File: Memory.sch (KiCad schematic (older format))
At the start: 22 parts, among them U10 74LS05, U11 74HCT00, U12 74LS27, U13 74HC74, U14 74HC86, U2 AS6C4008-55PCN, U3 AS6C4008-55PCN, U4 AS6C4008-55PCN, U5 AS6C4008-55PCN, U6 74HCT00, U7 74LS32, U8 74LS32, U9 74LS05

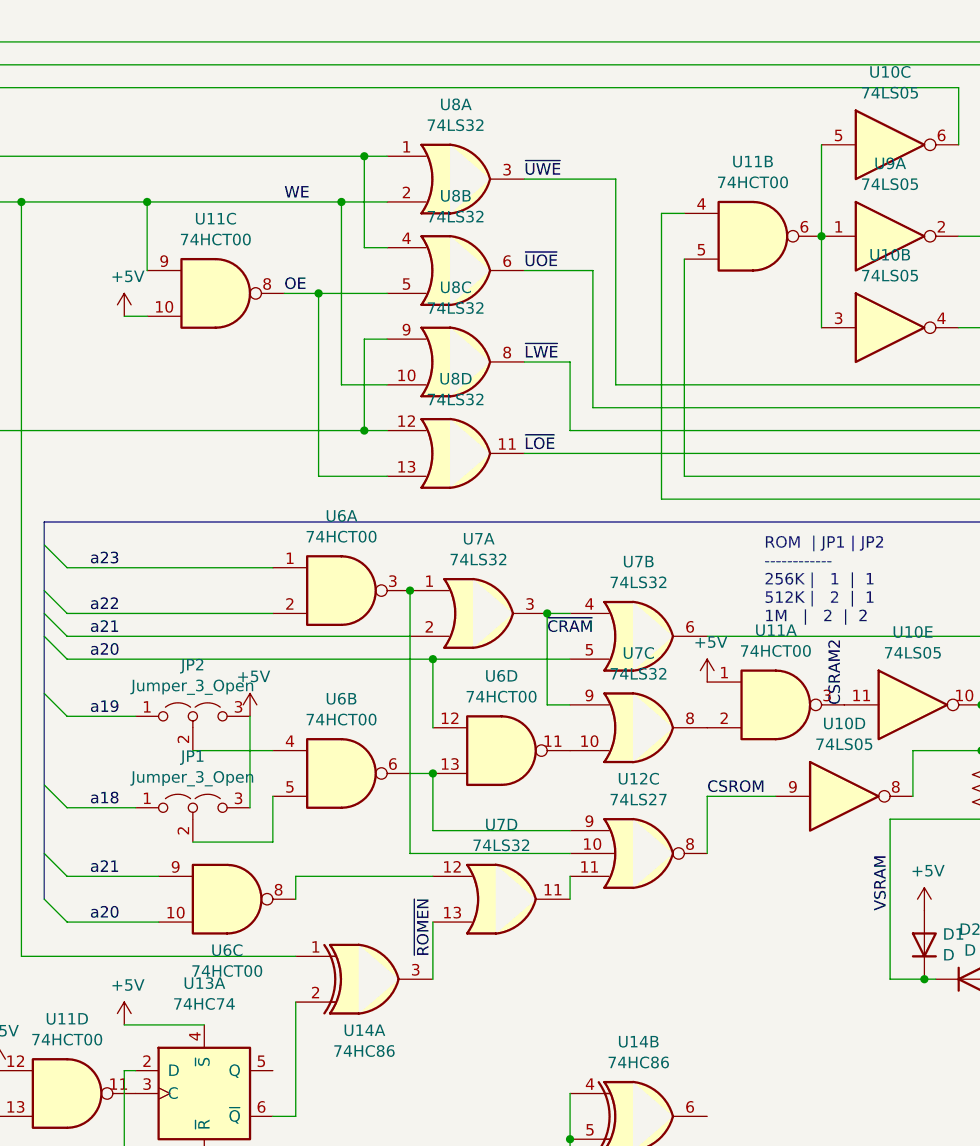
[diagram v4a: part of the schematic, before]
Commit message: reorganize components for partial builds
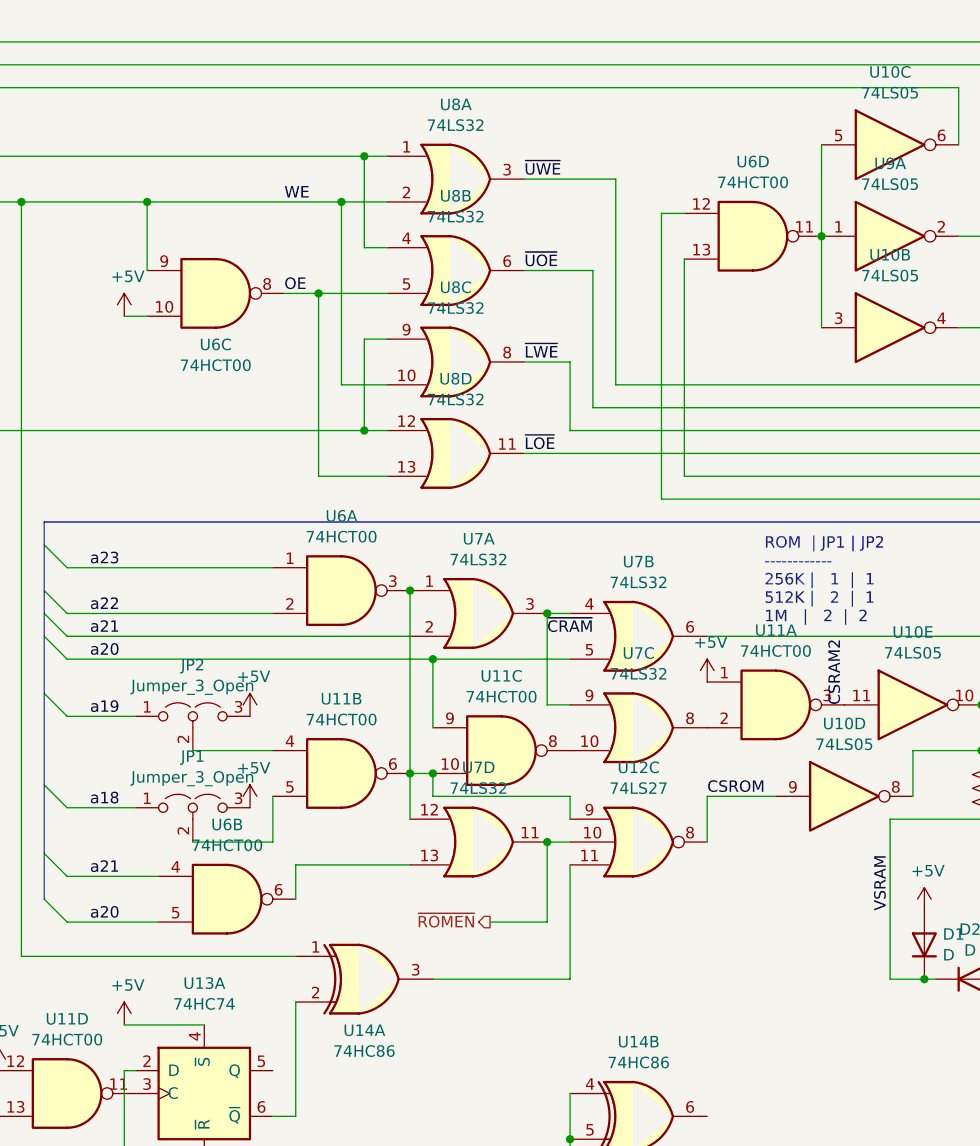
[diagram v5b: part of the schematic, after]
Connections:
- net +5V: now also U6.10; no longer U11.10
- net OE: now also U6.8; no longer U11.8
- net R~W: now also U6.9; no longer U11.9
- net a20: now also U11.9, U6.5; no longer U6.10, U6.12
- net a21: now also U6.4; no longer U6.9
- net ~CS1: now also U6.13; no longer U11.5
- net ~CS2: now also U6.12; no longer U11.4
- net ~ROMEN: now also U12.10, U7.11; no longer U14.3, U7.13
- net at JP2.2 (C): now also U11.4; no longer U6.4
- net at JP1.2 (C): now also U11.5; no longer U6.5
- net at U6.3, U7.1: now also U11.10, U11.6, U12.9, U7.12; no longer U12.10
- net at U12.11: now also U14.3; no longer U7.11
- net at U10.3, U10.5, U9.1: now also U6.11; no longer U11.6
- net at U7.10: now also U11.8; no longer U6.11
- new net: U6.6, U7.13
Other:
- moved on the sheet: U11B, U11C, U12C, U6B, U6C, U6D, U7D
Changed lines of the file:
@@
 L 74:74HCT00 U6
 U 2 1 6060E41B
-P 2600 3800
-F 0 "U6" H 2600 4125 50  0000 C CNN
-F 1 "74HCT00" H 2600 4034 50  0000 C CNN
-F 2 "" H 2600 3800 50  0001 C CNN
-F 3 "http://www.ti.com/lit/gpn/sn74hct00" H 2600 3800 50  0001 C CNN
-	2    2600 3800
+P 2100 4350
+F 0 "U6" H 2100 4675 50  0000 C CNN
+F 1 "74HCT00" H 2100 4584 50  0000 C CNN
+F 2 "" H 2100 4350 50  0001 C CNN
+F 3 "http://www.ti.com/lit/gpn/sn74hct00" H 2100 4350 50  0001 C CNN
+	2    2100 4350
 	1    0    0    -1
 $EndComp
@@
 L 74:74HCT00 U11
 U 3 1 61157704
-P 2050 1700
-F 0 "U11" H 2050 2025 50  0000 C CNN
-F 1 "74HCT00" H 2050 1934 50  0000 C CNN
-F 2 "" H 2050 1700 50  0001 C CNN
-F 3 "http://www.ti.com/lit/gpn/sn74hct00" H 2050 1700 50  0001 C CNN
-	3    2050 1700
+P 3300 3700
+F 0 "U11" H 3300 4025 50  0000 C CNN
+F 1 "74HCT00" H 3300 3934 50  0000 C CNN
+F 2 "" H 3300 3700 50  0001 C CNN
+F 3 "http://www.ti.com/lit/gpn/sn74hct00" H 3300 3700 50  0001 C CNN
+	3    3300 3700
 	1    0    0    -1
 $EndComp
@@
 L 74:74HCT00 U6
 U 4 1 61935EB2
-P 3300 3700
-F 0 "U6" H 3300 4025 50  0000 C CNN
-F 1 "74HCT00" H 3300 3934 50  0000 C CNN
-F 2 "" H 3300 3700 50  0001 C CNN
-F 3 "http://www.ti.com/lit/gpn/sn74hct00" H 3300 3700 50  0001 C CNN
-	4    3300 3700
+P 4400 1450
+F 0 "U6" H 4400 1775 50  0000 C CNN
+F 1 "74HCT00" H 4400 1684 50  0000 C CNN
+F 2 "" H 4400 1450 50  0001 C CNN
+F 3 "http://www.ti.com/lit/gpn/sn74hct00" H 4400 1450 50  0001 C CNN
+	4    4400 1450
 	1    0    0    -1
 $EndComp
@@
 Wire Wire Line
 	1950 3700 2300 3700
-Wire Wire Line
-	2200 3950 2200 3550
 Text Notes 4450 3150 0    50   ~ 0
 ROM  | JP1 | JP2\n------------\n256K |   1  |  1\n512K |   2  |  1\n1M   |   2  |  2
@@
 L 74:74HCT00 U11
 U 2 1 6192E8A1
-P 4400 1450
-F 0 "U11" H 4400 1775 50  0000 C CNN
-F 1 "74HCT00" H 4400 1684 50  0000 C CNN
-F 2 "" H 4400 1450 50  0001 C CNN
-F 3 "http://www.ti.com/lit/gpn/sn74hct00" H 4400 1450 50  0001 C CNN
-	2    4400 1450
+P 2600 3800
+F 0 "U11" H 2600 4125 50  0000 C CNN
+F 1 "74HCT00" H 2600 4034 50  0000 C CNN
+F 2 "" H 2600 3800 50  0001 C CNN
+F 3 "http://www.ti.com/lit/gpn/sn74hct00" H 2600 3800 50  0001 C CNN
+	2    2600 3800
 	1    0    0    -1
 $EndComp
@@
 	1    0    0    -1
 $EndComp
-Connection ~ 3000 3800
-Wire Wire Line
-	3000 3800 3000 4050
-Wire Wire Line
-	2900 3000 2900 4150
+Wire Wire Line
+	2900 3000 2900 3800
 Wire Wire Line
 	4300 5750 4300 5900
@@
 	1    0    0    -1
 $EndComp
-Text Label 3000 4600 1    50   ~ 0
-~ROMEN
 $Comp
 L 74:74HCT00 U6
 U 3 1 61932778
-P 2100 4350
-F 0 "U6" H 2100 4125 50  0000 C CNN
-F 1 "74HCT00" H 2100 4034 50  0000 C CNN
-F 2 "" H 2100 4350 50  0001 C CNN
-F 3 "http://www.ti.com/lit/gpn/sn74hct00" H 2100 4350 50  0001 C CNN
-	3    2100 4350
+P 2050 1700
+F 0 "U6" H 2050 1475 50  0000 C CNN
+F 1 "74HCT00" H 2050 1384 50  0000 C CNN
+F 2 "" H 2050 1700 50  0001 C CNN
+F 3 "http://www.ti.com/lit/gpn/sn74hct00" H 2050 1700 50  0001 C CNN
+	3    2050 1700
 	1    0    0    -1
 $EndComp
@@
 Text Label 4200 3900 0    50   ~ 0
 CSROM
-Wire Wire Line
-	3000 4450 3000 4700
-Wire Wire Line
-	4200 4150 4200 3900
-Wire Wire Line
-	3000 4050 3600 4050
-Wire Wire Line
-	3600 4250 3600 4350
-Wire Wire Line
-	2900 4150 3600 4150
 $Comp
 L 74:74LS27 U12
 U 3 1 61CF43AC
-P 3900 4150
-F 0 "U12" H 3900 4475 50  0000 C CNN
-F 1 "74LS27" H 3900 4384 50  0000 C CNN
-F 2 "" H 3900 4150 50  0001 C CNN
-F 3 "http://www.ti.com/lit/gpn/sn74LS27" H 3900 4150 50  0001 C CNN
-	3    3900 4150
+P 3900 4100
+F 0 "U12" H 3900 4425 50  0000 C CNN
+F 1 "74LS27" H 3900 4334 50  0000 C CNN
+F 2 "" H 3900 4100 50  0001 C CNN
+F 3 "http://www.ti.com/lit/gpn/sn74LS27" H 3900 4100 50  0001 C CNN
+	3    3900 4100
 	1    0    0    -1
 $EndComp
@@
 L 74:74LS32 U7
 U 4 1 6050398D
-P 3300 4350
-F 0 "U7" H 3300 4675 50  0000 C CNN
-F 1 "74LS32" H 3300 4584 50  0000 C CNN
-F 2 "" H 3300 4350 50  0001 C CNN
-F 3 "http://www.ti.com/lit/gpn/sn74LS32" H 3300 4350 50  0001 C CNN
-	4    3300 4350
+P 3200 4100
+F 0 "U7" H 3200 4425 50  0000 C CNN
+F 1 "74LS32" H 3200 4334 50  0000 C CNN
+F 2 "" H 3200 4100 50  0001 C CNN
+F 3 "http://www.ti.com/lit/gpn/sn74LS32" H 3200 4100 50  0001 C CNN
+	4    3200 4100
 	1    0    0    -1
 $EndComp
@@
 Wire Wire Line
 	3500 6500 4200 6500
-Wire Wire Line
-	2400 4350 2400 4250
-Wire Wire Line
-	2400 4250 3000 4250
 $Comp
 L RAM:AS6C4008-55PCN U?
@@
 Wire Wire Line
 	1650 5100 1700 5100
+$Comp
+L OpenAmiga2000CoproAdapter-rescue:+5V-power #PWR?
+U 1 1 621BDE0A
+P 2200 3950
+AR Path="/621BDE0A" Ref="#PWR?"  Part="1"
+AR Path="/6068F728/621BDE0A" Ref="#PWR?"  Part="1"
+F 0 "#PWR?" H 2200 3800 50  0001 C CNN
+F 1 "+5V" H 2215 4123 50  0000 C CNN
+F 2 "" H 2200 3950 50  0001 C CNN
+F 3 "" H 2200 3950 50  0001 C CNN
+	1    2200 3950
+	1    0    0    -1
+$EndComp
+Wire Wire Line
+	3000 3800 3000 3900
+Wire Wire Line
+	3000 3900 3600 3900
+Wire Wire Line
+	3600 3900 3600 4000
+Connection ~ 3000 3800
+Wire Wire Line
+	4200 4100 4200 3900
+Wire Wire Line
+	2400 4200 2400 4350
+Wire Wire Line
+	3000 4700 3600 4700
+Wire Wire Line
+	3600 4200 3600 4700
+Wire Wire Line
+	2900 4200 2400 4200
+Wire Wire Line
+	3500 4100 3600 4100
+Wire Wire Line
+	3500 4100 3500 4450
+Wire Wire Line
+	3500 4450 3250 4450
 Wire Bus Line
 	1300 2700 1300 4350
@@
 Wire Bus Line
 	8900 600  8900 5950
+Connection ~ 3500 4100
+Text HLabel 3250 4450 0    50   Output ~ 0
+~ROMEN
+Connection ~ 2900 3800
+Wire Wire Line
+	2900 3800 2900 4000
 $EndSCHEMATC

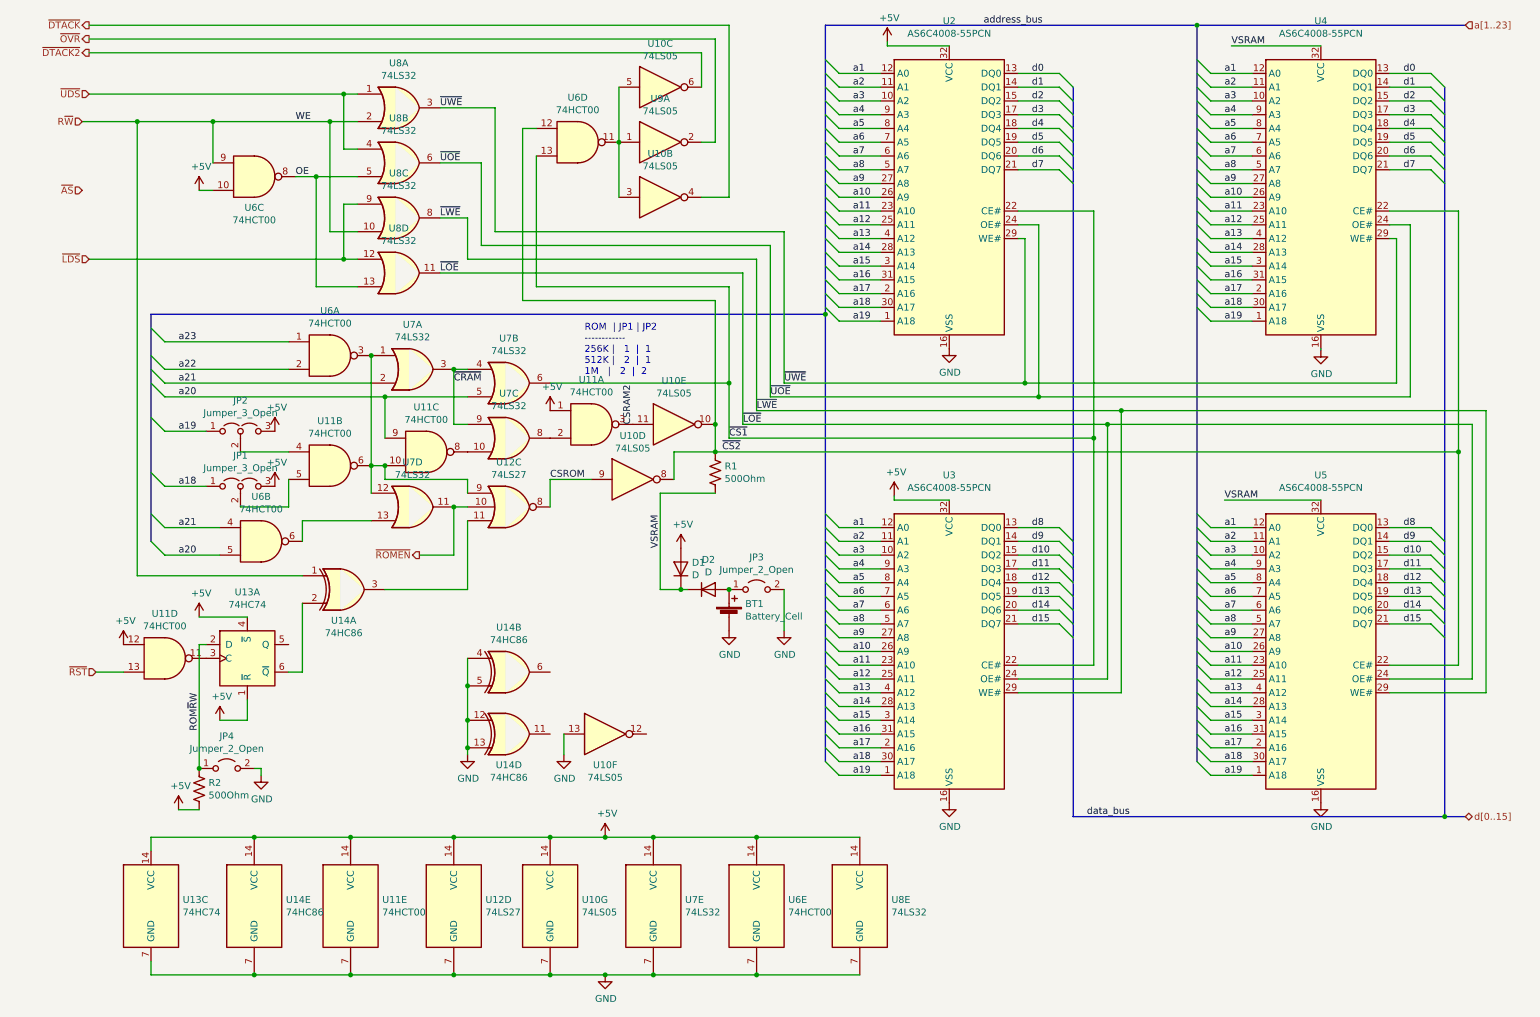
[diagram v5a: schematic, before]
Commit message: add jumpers to disable memory banks
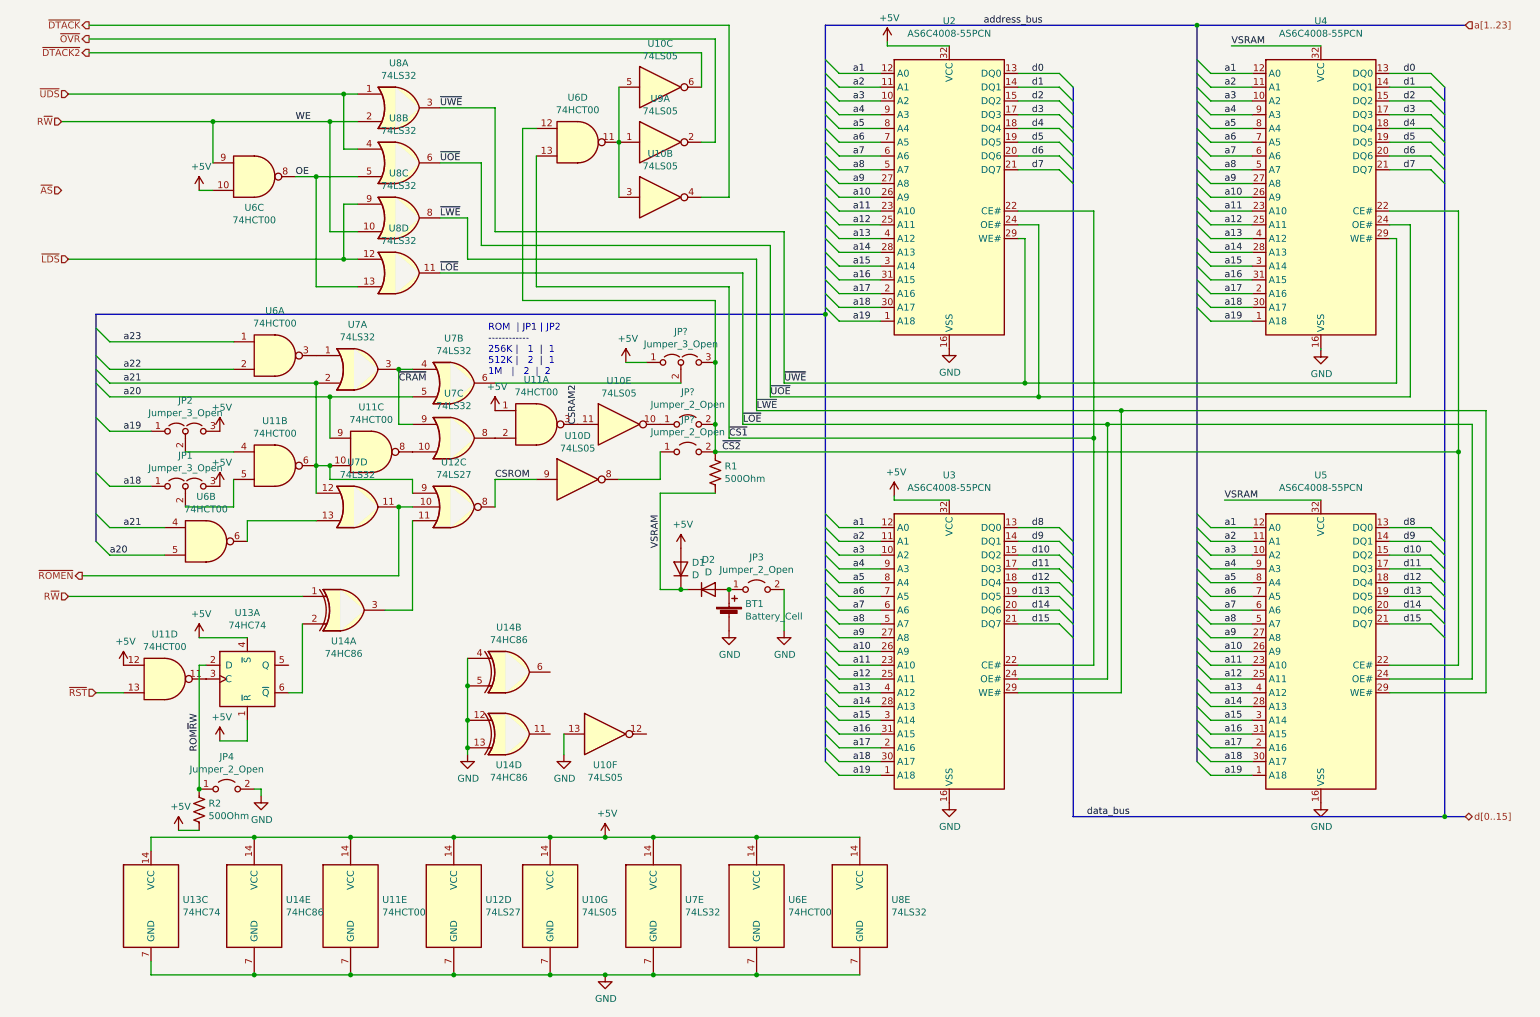
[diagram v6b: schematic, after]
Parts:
- added JP? (x2): Jumper_2_Open, symbol jumper:Jumper_2_Open
- added JP?: Jumper_3_Open, symbol jumper:Jumper_3_Open
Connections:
- net +5V: now also JP?.1 (A)
- net a21: now also U11.10, U11.6, U12.9, U7.12
- net ~CS1: no longer U7.6
- net ~CS2: now also JP?.2 (B), JP?.2 (B), JP?.3 (B); no longer U10.10, U10.8
- new net: JP?.1 (A), U10.10
- new net: JP?.1 (A), U10.8
- new net: JP?.2 (C), U7.6
- new net: U6.3, U7.1
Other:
- moved on the sheet: JP1, JP2, JP4, R2, U10D, U10E, U11A, U11B, U11C, U11D, U12C, U13A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

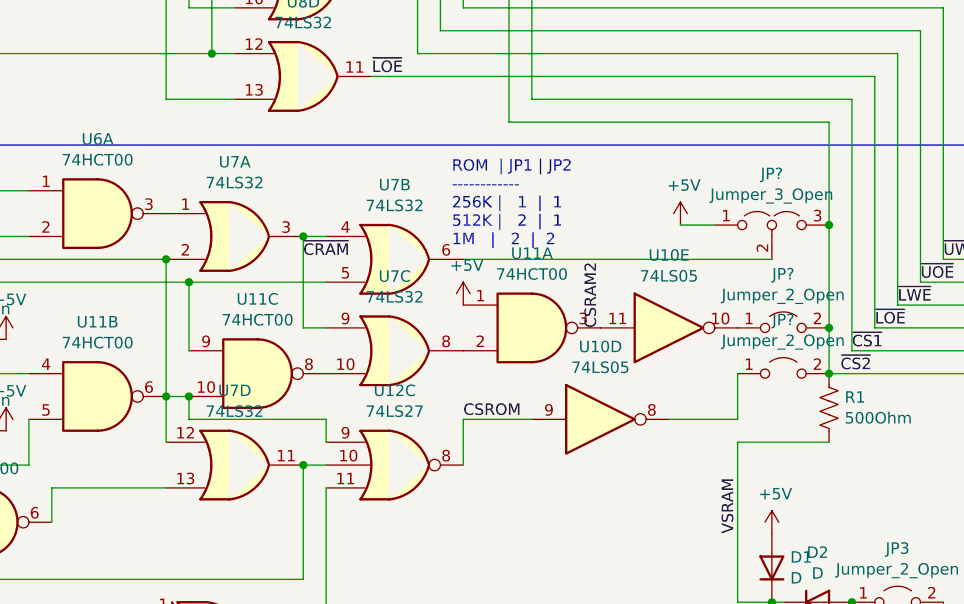
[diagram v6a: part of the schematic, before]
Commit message: remove wrong connection
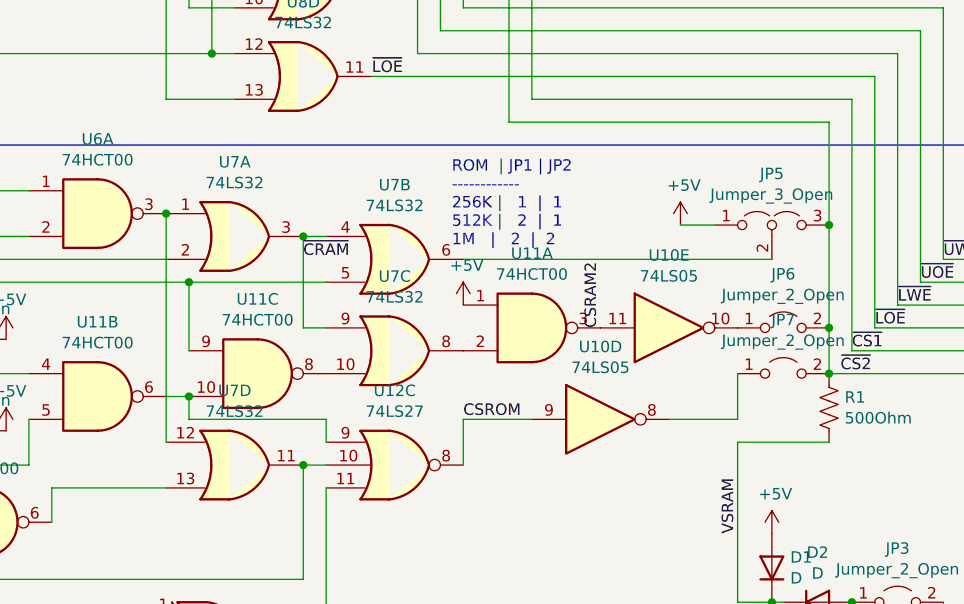
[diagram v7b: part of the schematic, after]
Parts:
- gave numbers to parts that had none: 3
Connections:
- net a21: no longer U11.10, U11.6, U12.9, U7.12
- net at U6.3, U7.1: now also U7.12
- new net: U11.10, U11.6, U12.9
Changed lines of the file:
@@
 P 1100 5250
 AR Path="/6217CE2E" Ref="#PWR?"  Part="1"
-AR Path="/6068F728/6217CE2E" Ref="#PWR?"  Part="1"
-F 0 "#PWR?" H 1100 5100 50  0001 C CNN
+AR Path="/6068F728/6217CE2E" Ref="#PWR0120"  Part="1"
+F 0 "#PWR0120" H 1100 5100 50  0001 C CNN
 F 1 "+5V" H 1115 5423 50  0000 C CNN
 F 2 "" H 1100 5250 50  0001 C CNN
@@
 P 1800 3950
 AR Path="/621BDE0A" Ref="#PWR?"  Part="1"
-AR Path="/6068F728/621BDE0A" Ref="#PWR?"  Part="1"
-F 0 "#PWR?" H 1800 3800 50  0001 C CNN
+AR Path="/6068F728/621BDE0A" Ref="#PWR0122"  Part="1"
+F 0 "#PWR0122" H 1800 3800 50  0001 C CNN
 F 1 "+5V" H 1815 4123 50  0000 C CNN
 F 2 "" H 1800 3950 50  0001 C CNN
@@
 Text HLabel 800  4600 0    50   Output ~ 0
 ~ROMEN
-Connection ~ 2500 3800
-Wire Wire Line
-	2500 3800 2500 4000
-Wire Wire Line
-	2500 3200 2500 3800
-Connection ~ 2500 3200
 Wire Wire Line
 	5500 2500 5500 3600
@@
 	5400 2600 5400 3050
 $Comp
-L jumper:Jumper_2_Open JP?
+L jumper:Jumper_2_Open JP6
 U 1 1 601397C6
 P 5200 3500
-F 0 "JP?" H 5200 3735 50  0000 C CNN
+F 0 "JP6" H 5200 3735 50  0000 C CNN
 F 1 "Jumper_2_Open" H 5200 3644 50  0000 C CNN
 F 2 "" H 5200 3500 50  0001 C CNN
@@
 	1000 4450 1400 4450
 $Comp
-L jumper:Jumper_2_Open JP?
+L jumper:Jumper_2_Open JP7
 U 1 1 601E25A4
 P 5200 3700
-F 0 "JP?" H 5200 3935 50  0000 C CNN
+F 0 "JP7" H 5200 3935 50  0000 C CNN
 F 1 "Jumper_2_Open" H 5200 3844 50  0000 C CNN
 F 2 "" H 5200 3700 50  0001 C CNN
@@
 	900  2700 6200 2700
 $Comp
-L jumper:Jumper_3_Open JP?
+L jumper:Jumper_3_Open JP5
 U 1 1 602480DF
 P 5150 3050
-F 0 "JP?" H 5150 3274 50  0000 C CNN
+F 0 "JP5" H 5150 3274 50  0000 C CNN
 F 1 "Jumper_3_Open" H 5150 3183 50  0000 C CNN
 F 2 "" H 5150 3050 50  0001 C CNN
@@
 P 4750 3050
 AR Path="/6026A4ED" Ref="#PWR?"  Part="1"
-AR Path="/6068F728/6026A4ED" Ref="#PWR?"  Part="1"
-F 0 "#PWR?" H 4750 2900 50  0001 C CNN
+AR Path="/6068F728/6026A4ED" Ref="#PWR0123"  Part="1"
+F 0 "#PWR0123" H 4750 2900 50  0001 C CNN
 F 1 "+5V" H 4765 3223 50  0000 C CNN
 F 2 "" H 4750 3050 50  0001 C CNN
@@
 Wire Wire Line
 	800  4600 3100 4600
+Wire Wire Line
+	3100 4100 3100 4600
 Wire Bus Line
 	900  2700 900  4350
@@
 Wire Bus Line
 	8900 600  8900 5950
+Connection ~ 2500 3000
 Wire Wire Line
-	3100 4100 3100 4600
+	2500 3000 2500 4000
 $EndSCHEMATC
